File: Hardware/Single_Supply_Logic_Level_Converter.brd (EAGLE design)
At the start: 25.4 x 27.9 mm, 73 parts, among them U1 TXB0104, U2 TPS61200, U3 ADJ

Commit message: Updates per Engineering Design Review
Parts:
- removed FD3: FIDUCIALUFIDUCIAL, SparkFun-Aesthetics:FIDUCIAL-MICRO
- added U$44: (no value), buzzard_labels (92):VOUT2
- added U$47: (no value), buzzard_labels (99):VCCA_DFLT_#_3#3V0
- added U$48: (no value), buzzard_labels (100):VCCB_#_5V0
- added U$49: (no value), buzzard_labels:R10
- added U$56: (no value), buzzard_labels (93):VCCB_#_5V1
- added U$8: (no value), buzzard_labels (92):VIN1
- U$27: device buzzard_labels (84):VOUT1 -> buzzard_labels (92):VOUT2
- U$36: device buzzard_labels (84):VIN0 -> buzzard_labels (95):VCCA_#_3#3V0
- U$38: device buzzard_labels (84):VIN0 -> buzzard_labels (92):VIN1
- moved FD4 16.4 mm to (6.83, 1.11)
- moved U$36 13.2 mm to (-0.69, 13.5)
- moved LOGO2 12.9 mm to (3.53, 16.1)
- moved U$27 6.22 mm to (25.4, 26.7), flipped to the bottom
- moved U$38 4.69 mm to (-0.25, 26.7), flipped to the top
- moved D1 3.99 mm to (18.4, 5.89), turned to 90 degrees
- moved U$29 3.63 mm to (16.0, 3.60)
- moved U$16 2.54 mm to (5.40, 1.27)
- moved U$15 2.54 mm to (5.42, 3.81)
- moved J3 2.54 mm to (1.27, 11.4)
- moved J4 2.54 mm to (24.1, 11.4)
- moved U$18 2.54 mm to (23.3, 6.35)
- moved U$19 2.54 mm to (20.0, 6.35)
- moved U$24 2.54 mm to (2.11, 11.4)
- moved U$34 2.54 mm to (19.4, 11.4)
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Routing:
- net N$11: track 19.7 -> 13.1 mm
- net B4: track 11.4 -> 15.6 mm
- net A4: track 11.4 -> 15.0 mm
- net A3: track 10.6 -> 13.1 mm
- net 5V: track 35.7 -> 38.1 mm
- net B3: track 10.6 -> 12.4 mm
- net A2: track 9.83 -> 10.9 mm
- net B2: track 9.83 -> 10.9 mm
- net B1: track 9.05 -> 10.1 mm
- net A1: track 9.05 -> 10.1 mm
- net VCCA: track 61.4 -> 60.5 mm
- net N$3: track 3.01 -> 3.79 mm
- net GND: vias 12 -> 13

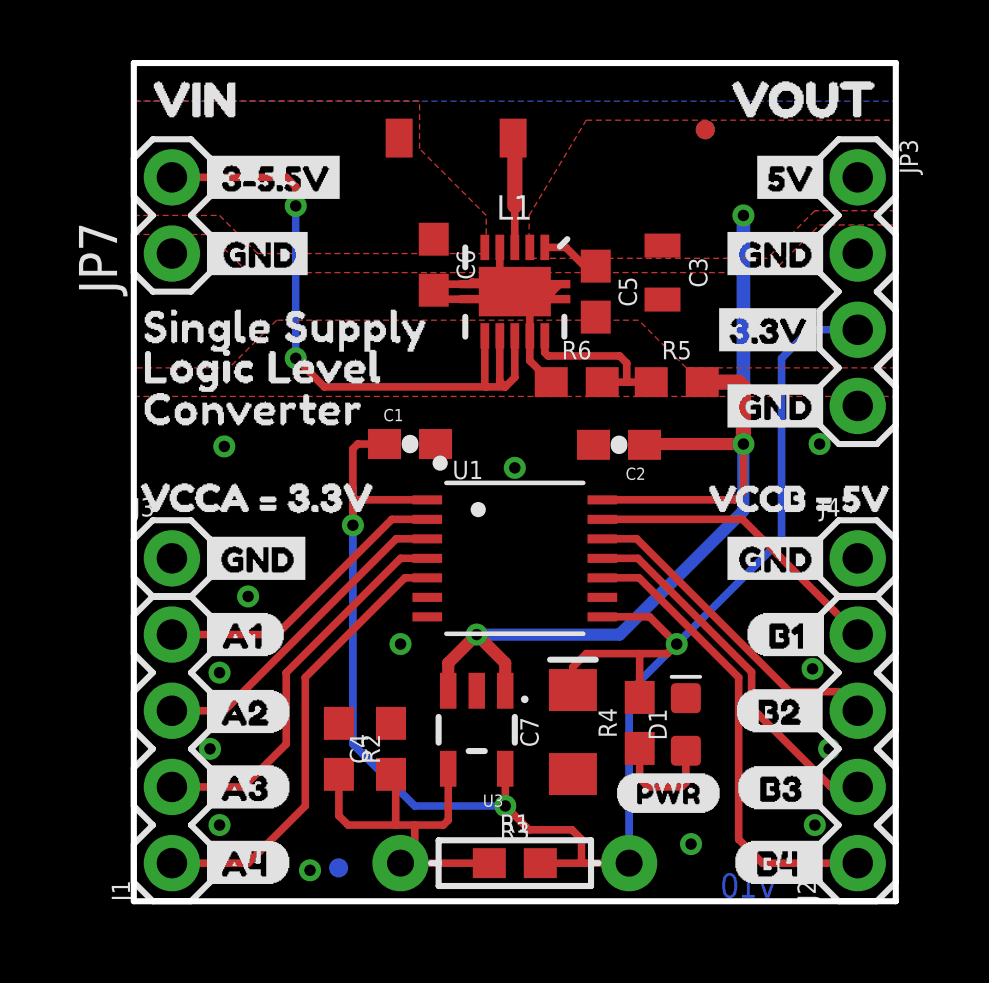
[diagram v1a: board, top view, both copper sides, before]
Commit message: Adding a lost fiducial
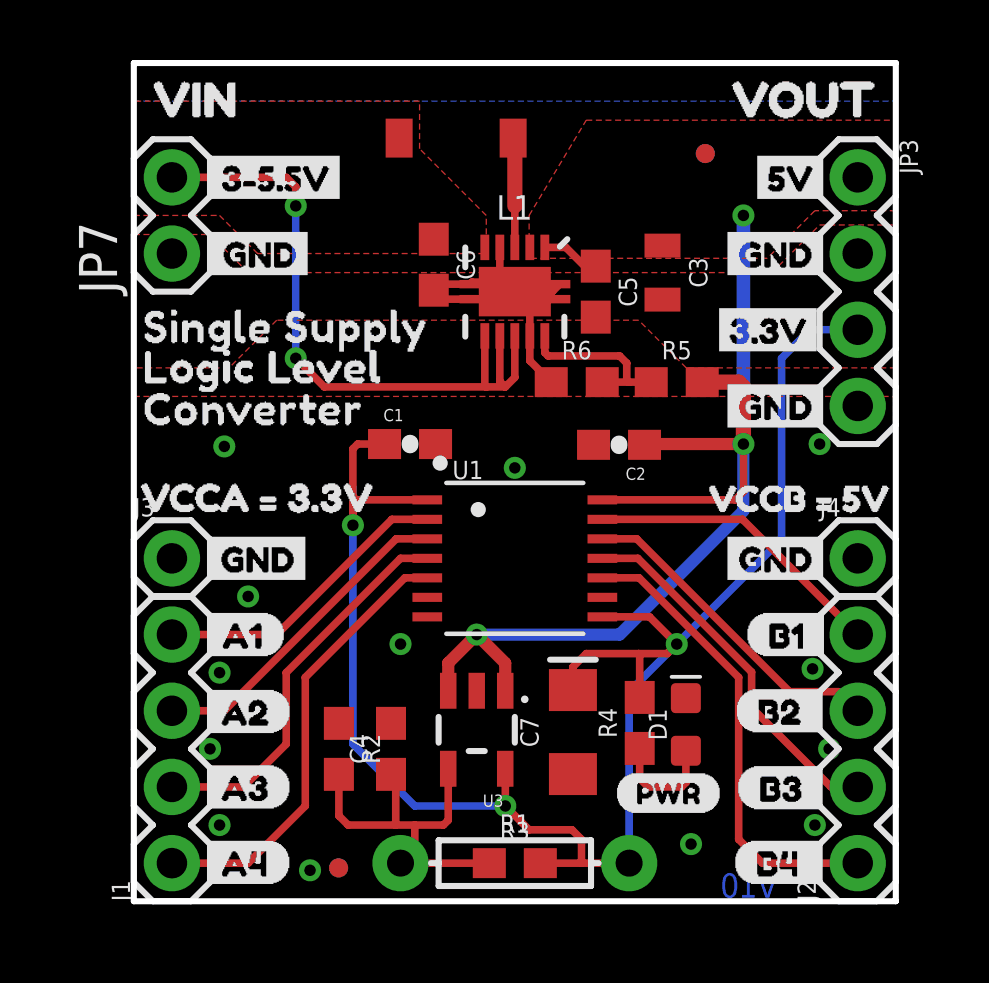
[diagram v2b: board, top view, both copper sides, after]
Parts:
- added FD3: FIDUCIALUFIDUCIAL, SparkFun-Aesthetics:FIDUCIAL-MICRO
- moved FD1 0.79 mm to (19.1, 24.9)
- moved FD2 0.79 mm to (19.1, 24.9)
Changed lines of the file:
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@@
 <attribute name="PROD_ID" value="CAP-07884" x="8.5725" y="5.08" size="1.778" layer="27" rot="R90" display="off"/>
 </element>
-<element name="FD1" library="SparkFun-Aesthetics" package="FIDUCIAL-MICRO" value="FIDUCIALUFIDUCIAL" x="19.05" y="25.7175"/>
-<element name="FD2" library="SparkFun-Aesthetics" package="FIDUCIAL-MICRO" value="FIDUCIALUFIDUCIAL" x="19.05" y="25.7175" rot="MR0"/>
+<element name="FD1" library="SparkFun-Aesthetics" package="FIDUCIAL-MICRO" value="FIDUCIALUFIDUCIAL" x="19.05" y="24.92375"/>
+<element name="FD2" library="SparkFun-Aesthetics" package="FIDUCIAL-MICRO" value="FIDUCIALUFIDUCIAL" x="19.05" y="24.92375" rot="MR0"/>
 <element name="FD4" library="SparkFun-Aesthetics" package="FIDUCIAL-MICRO" value="FIDUCIALUFIDUCIAL" x="6.82625" y="1.11125" rot="MR0"/>
 <element name="C7" library="SparkFun-Capacitors" package="EIA3216" value="10uF" x="14.63675" y="5.6388" rot="R90">
@@
 <element name="U$48" library="buzzard_labels (100)" package="VCCB_#_5V0" value="" x="16.5862" y="9.4234" rot="MR0"/>
 <element name="U$49" library="buzzard_labels" package="R10" value="" x="14.224" y="1.2446" rot="MR0"/>
+<element name="FD3" library="SparkFun-Aesthetics" package="FIDUCIAL-MICRO" value="FIDUCIALUFIDUCIAL" x="6.82625" y="1.11125"/>
 </elements>
 <signals>

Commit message: updated MIC5205(ADJ) part
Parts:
- U3: value ADJ -> MIC5205(ADJ)
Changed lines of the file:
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@@
 </element>
 <element name="LOGO1" library="SparkFun-Aesthetics" package="SFE_LOGO_NAME_FLAME_.1" value="SFE_LOGO_NAME_FLAME.1_INCH" x="18.415" y="19.05" rot="MR0"/>
-<element name="U3" library="SparkFun-IC-Power" package="SOT23-5" value="ADJ" x="11.43" y="5.715" rot="R180">
+<element name="U3" library="SparkFun-IC-Power" package="SOT23-5" value="MIC5205(ADJ)" x="11.43" y="5.715" rot="R180">
 <attribute name="PROD_ID" value="VREG-12594" x="11.43" y="5.715" size="1.778" layer="27" rot="R180" display="off"/>
 </element>
